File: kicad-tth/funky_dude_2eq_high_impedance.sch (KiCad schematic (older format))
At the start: 32 parts, among them P1 CONN_2, P2 CONN_2, P3 CONN_2, U1 LM833

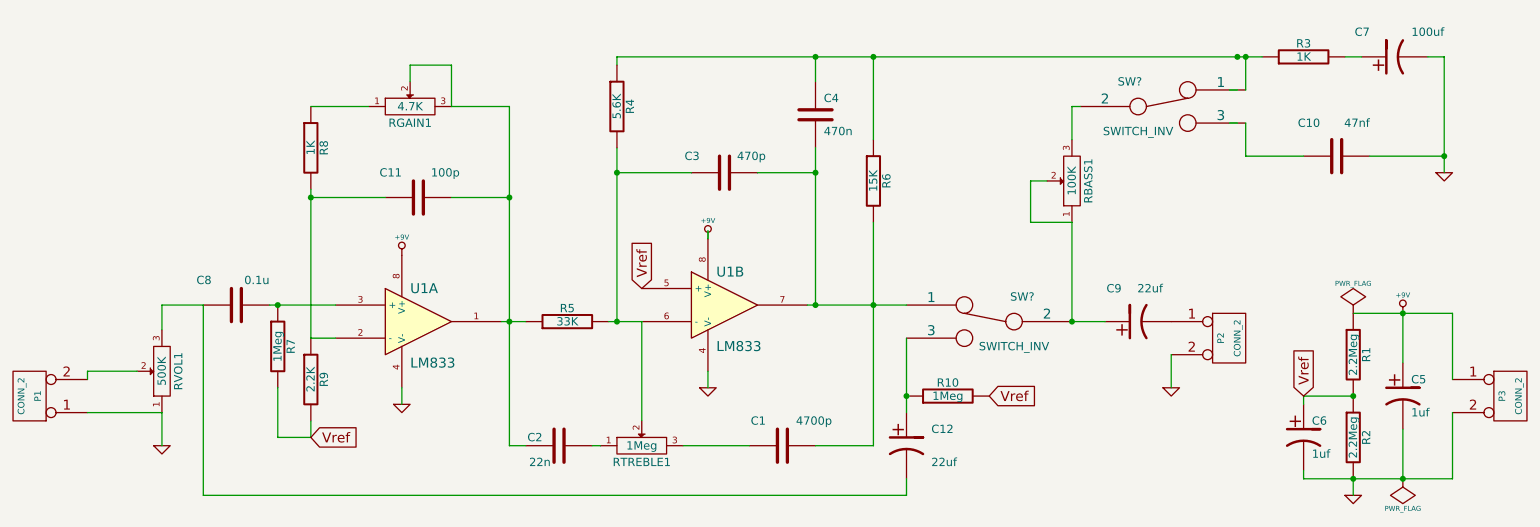
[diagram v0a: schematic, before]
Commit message: separate smd and tth projects
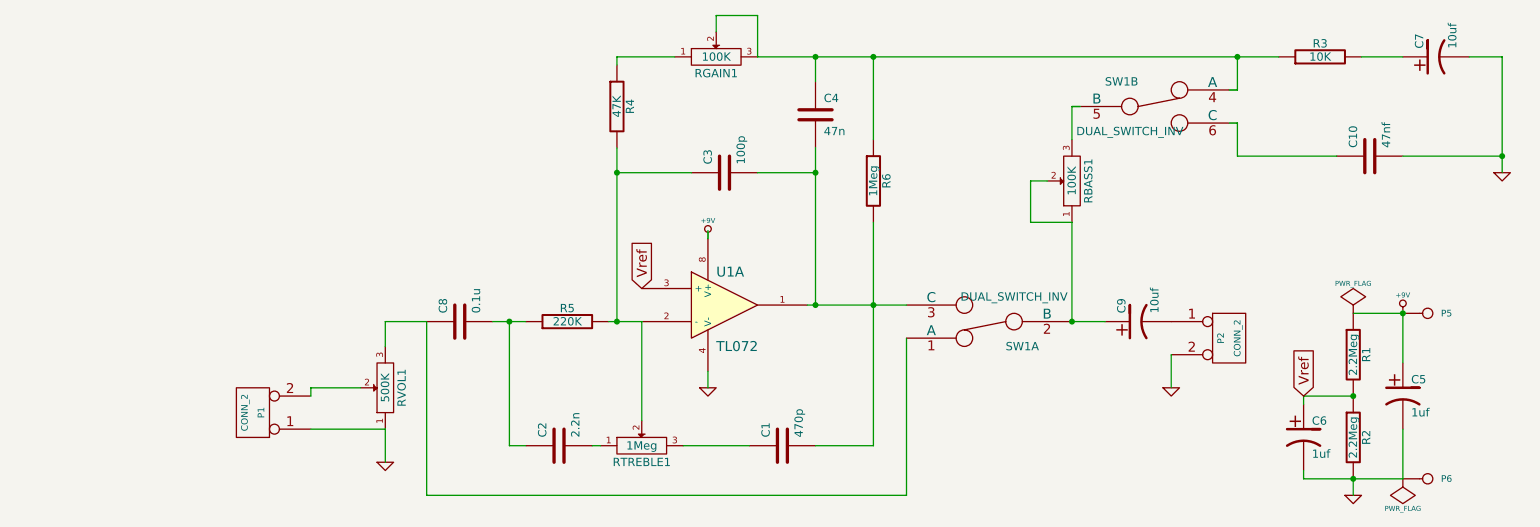
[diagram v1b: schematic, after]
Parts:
- removed C11: 100p, symbol C
- removed C12: 22uf, symbol CP1
- removed P3: CONN_2, symbol CONN_2
- removed R10, R7: 1Meg, symbol R
- removed R8: 1K, symbol R
- removed R9: 2.2K, symbol R
- removed SW? (x2): SWITCH_INV, symbol SWITCH_INV
- removed unit 1 of U1
- added P5, P6: CONN_1, symbol CONN_1
- added SW1: DUAL_SWITCH_INV, symbol DUAL_SWITCH_INV
- C1: value 4700p -> 470p
- C2: value 22n -> 2.2n
- C3: value 470p -> 100p
- C4: value 470n -> 47n
- C7: value 100uf -> 10uf
- C9: value 22uf -> 10uf
- R3: value 1K -> 10K
- R4: value 5.6K -> 47K
- R5: value 33K -> 220K
- R6: value 15K -> 1Meg
- RGAIN1: value 4.7K -> 100K
- U1: value LM833 -> TL072
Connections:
- wire segments 91 -> 58
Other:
- moved on the sheet: C10, C7, C8, P1, R3, RGAIN1, RVOL1
